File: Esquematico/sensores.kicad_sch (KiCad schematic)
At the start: 2 parts, among them U2 DS18B20

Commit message: sensores 1
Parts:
- added C1: 10u, symbol Device:C
- added C2: 0.1u, symbol Device:C
- added R? (x2): R, symbol Device:R
- added U2: MAX98357AETE+, QFN50P300X300X80-17N, symbol MAX98357AETE_:MAX98357AETE+
- added U?: SR501, symbol Sensor_Luz:SR501
- added U?: SEN0193, symbol Sensor_Luz:SR501
- added U?: APSD-9960-Ar, symbol Sensor_Luz:APSD-9960-Ar
- renumbered U2 to U1
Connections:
- net +5V: now also C1.1, C2.1, U2.2 (GAIN_SLOT), U2.7 (VDD), U2.8 (VDD), U?.1 (Vcc), U?.1 (Vcc)
- net GND: now also C1.2, C2.2, U2.11 (GND), U2.15 (GND), U2.3 (GND), U?.2 (GND), U?.3 (GND), U?.3 (GND)
- new net +3V3: R?.1, R?.1, U?.3 (VCC)
- new net INT: U?.6 (INT)
- new net SCL: R?.2, U?.5 (SCL)
- new net SDA: R?.2, U?.4 (SDA)
- new net VL: U?.1 (VL)
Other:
- note added: "Amplificador de sonido"
- note added: "Sensor de humedad"
- note added: "Sensor de luz"
- note added: "Sensor de moviemiento"
- moved on the sheet: R1, U1

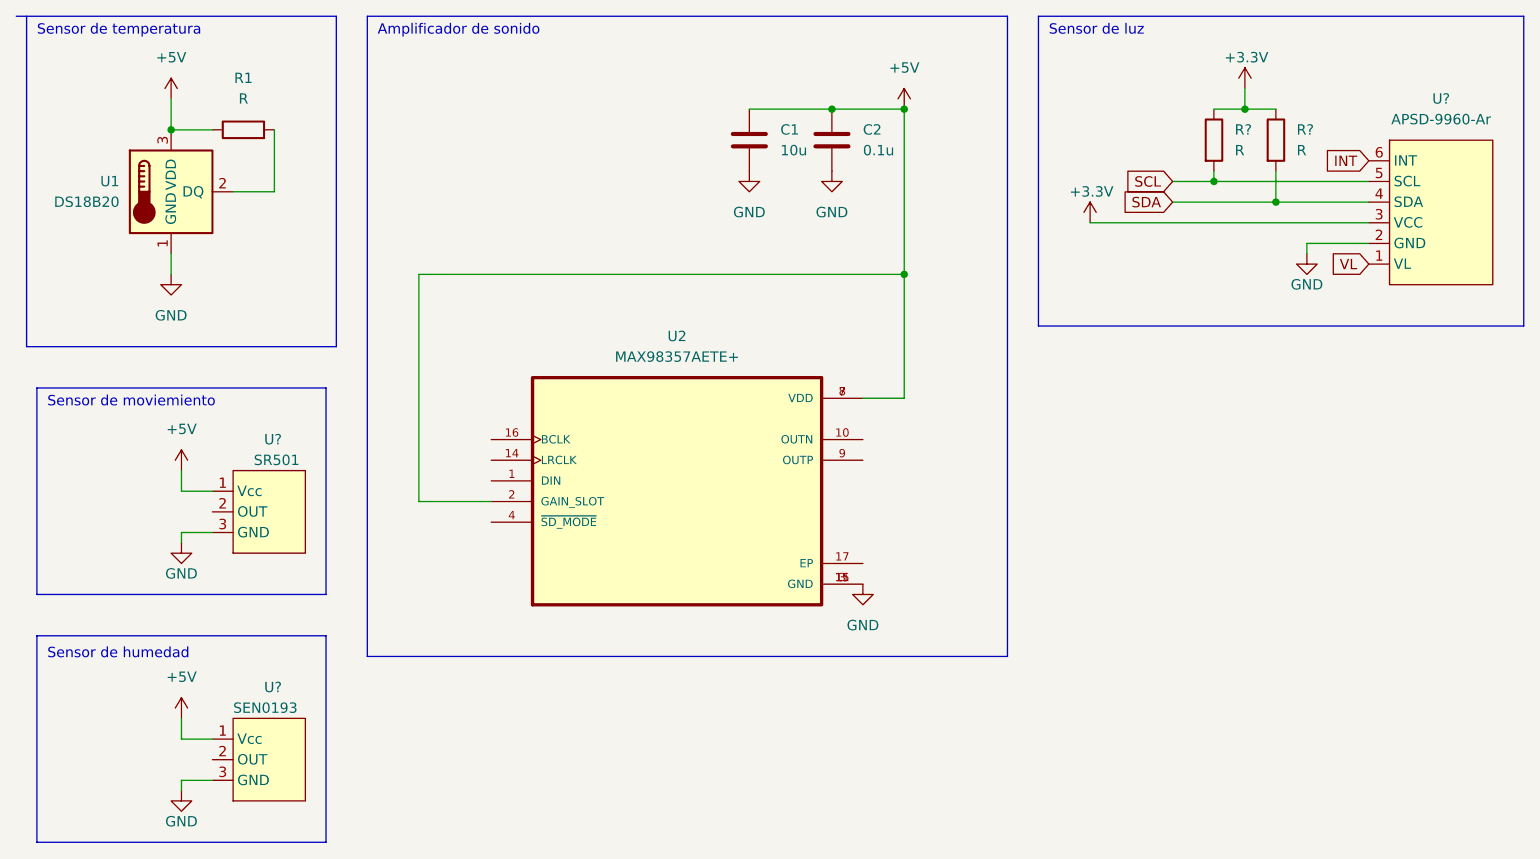
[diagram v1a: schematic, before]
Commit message: Conexion Sensores
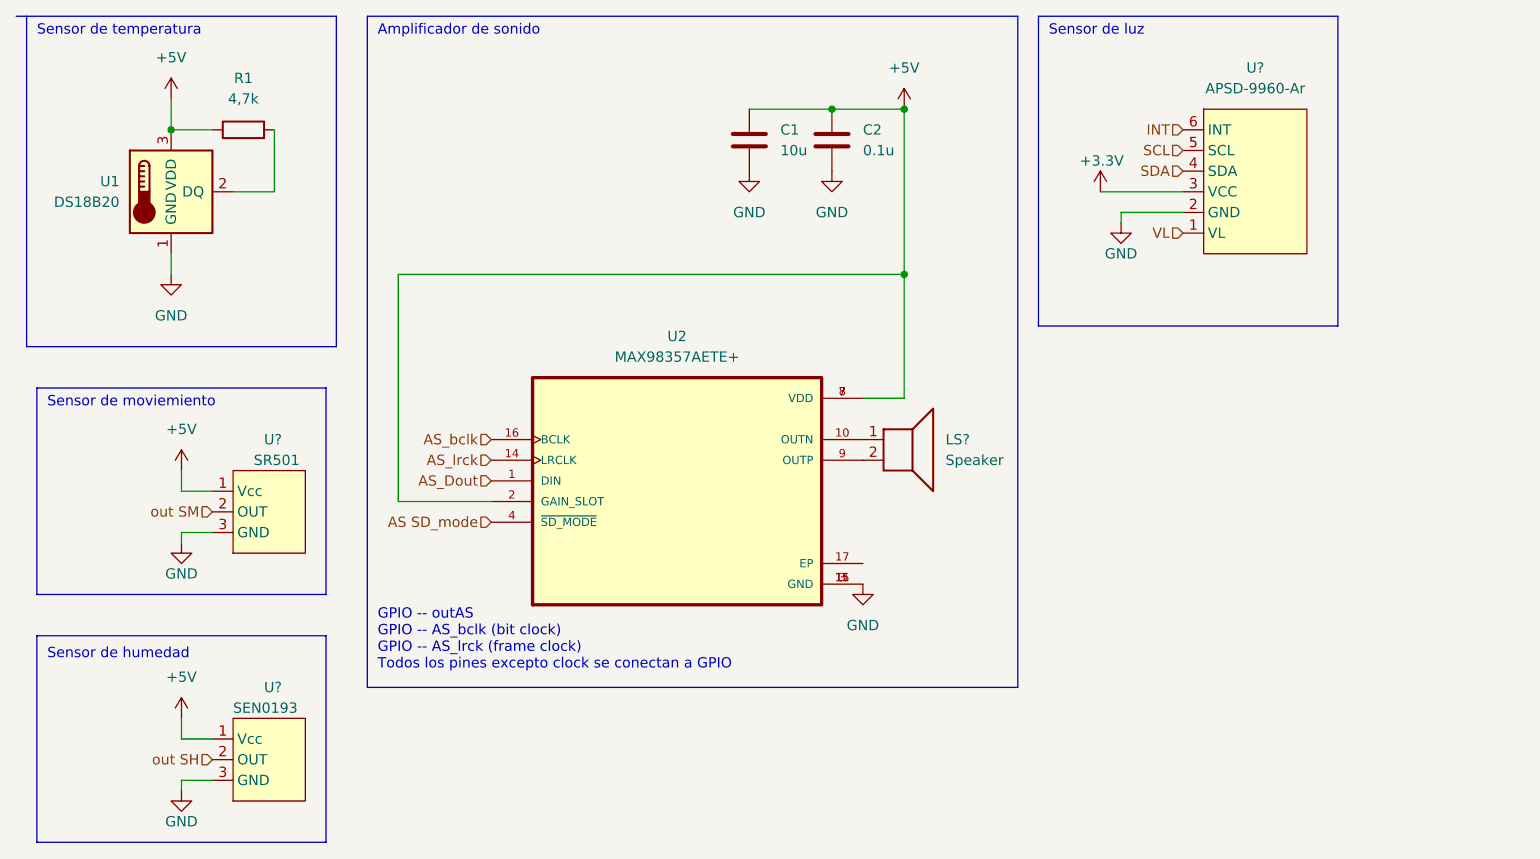
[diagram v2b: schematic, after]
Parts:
- removed R? (x2): R, symbol Device:R
- added LS?: Speaker, symbol Device:Speaker
- R1: value R -> 4,7k
- U?: footprint (none) -> Connector_JST:JST_PH_B3B-PH-SM4-TB_1x03-1MP_P2.00mm_Vertical
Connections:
- net AS_Dout: now reaches U2.1 (DIN)
- net at U2.10 (OUTN): now also LS?.1
- net AS_lrck: now reaches U2.14 (LRCLK)
- net AS_bclk: now reaches U2.16 (BCLK)
- net AS SD_mode: now reaches U2.4 (~{SD_MODE})
- net at U2.9 (OUTP): now also LS?.2
- net out SM: now reaches U?.2 (OUT)
- net out SH: now reaches U?.2 (OUT)
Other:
- note added: "GPIO -- outAS GPIO -- AS_bclk (bit clock) GPIO -- AS_lrck (frame clock) Todos los pines excepto clock se conectan a GPIO"
- moved on the sheet: U?

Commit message: actualizacion huellas resitencias y capacitorees
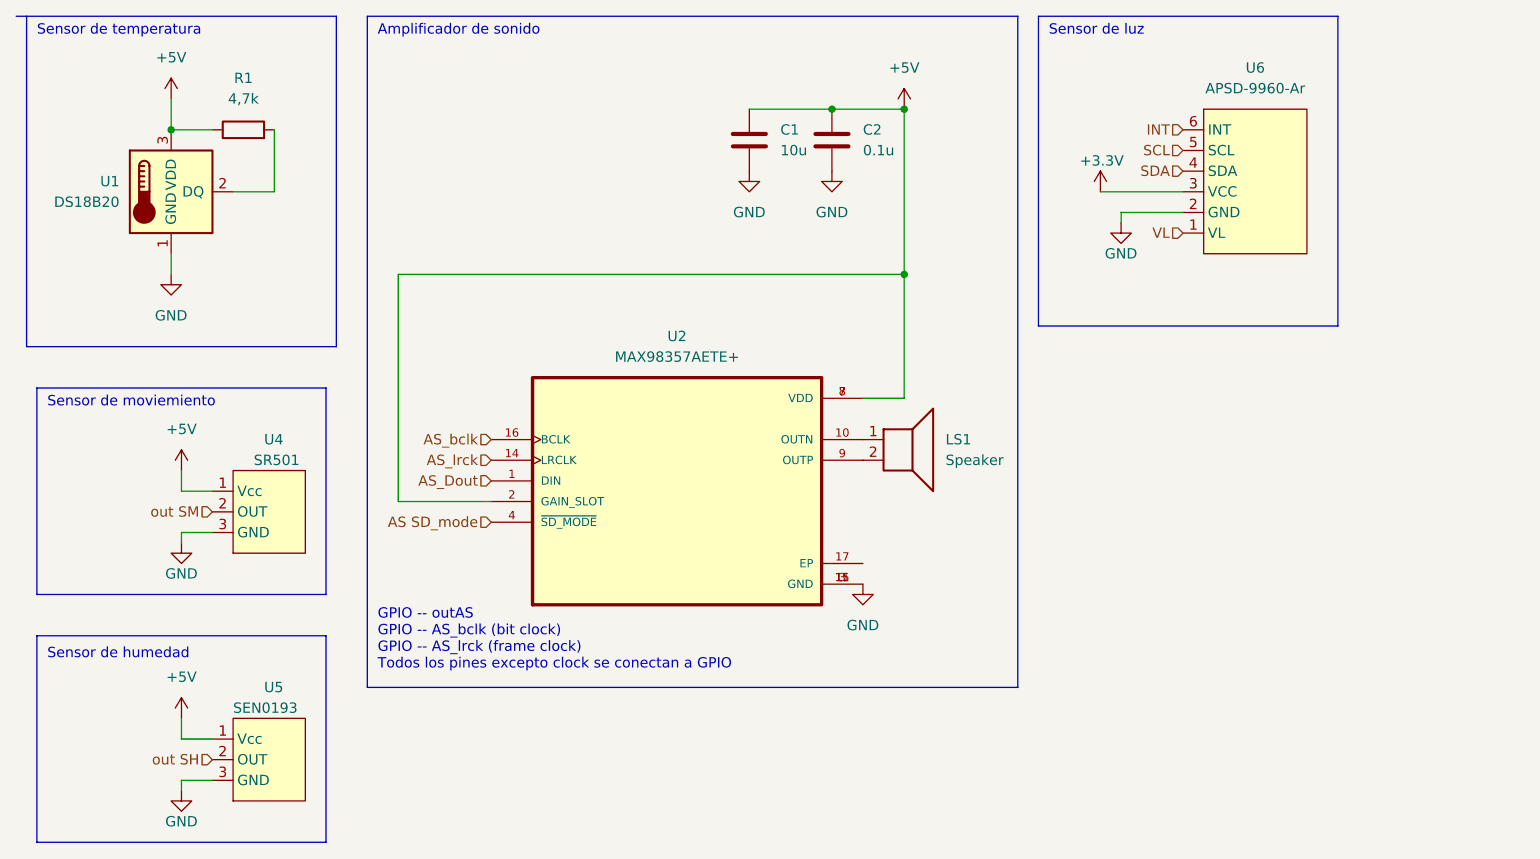
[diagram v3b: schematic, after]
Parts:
- C1, C2: footprint (none) -> Capacitor_SMD:C_0805_2012Metric_Pad1.18x1.45mm_HandSolder
- R1: footprint (none) -> Resistor_SMD:R_0805_2012Metric_Pad1.20x1.40mm_HandSolder
- gave numbers to parts that had none: 4
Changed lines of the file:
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@@
   (symbol (lib_id "power:+5V") (at 39.37 105.41 0) (unit 1)
     (in_bom yes) (on_board yes) (fields_autoplaced)
-    (property "Reference" "#PWR?" (id 0) (at 39.37 109.22 0)
+    (property "Reference" "#PWR0128" (id 0) (at 39.37 109.22 0)
       (effects (font (size 1.27 1.27)) hide)
     )
@@
     (property "Reference" "R1" (id 0) (at 46.99 26.67 90))
     (property "Value" "4,7k" (id 1) (at 46.99 29.21 90))
-    (property "Footprint" "" (id 2) (at 46.99 34.798 90)
+    (property "Footprint" "Resistor_SMD:R_0805_2012Metric_Pad1.20x1.40mm_HandSolder" (id 2) (at 46.99 34.798 90)
       (effects (font (size 1.27 1.27)) hide)
     )
@@
   (symbol (lib_id "power:GND") (at 39.37 114.3 0) (unit 1)
     (in_bom yes) (on_board yes)
-    (property "Reference" "#PWR?" (id 0) (at 39.37 120.65 0)
+    (property "Reference" "#PWR0127" (id 0) (at 39.37 120.65 0)
       (effects (font (size 1.27 1.27)) hide)
     )
@@
       (effects (font (size 1.27 1.27)) (justify left))
     )
-    (property "Footprint" "" (id 2) (at 110.1852 38.1 0)
+    (property "Footprint" "Capacitor_SMD:C_0805_2012Metric_Pad1.18x1.45mm_HandSolder" (id 2) (at 110.1852 38.1 0)
       (effects (font (size 1.27 1.27)) hide)
     )
@@
   (symbol (lib_id "power:GND") (at 123.19 88.9 0) (unit 1)
     (in_bom yes) (on_board yes) (fields_autoplaced)
-    (property "Reference" "#PWR?" (id 0) (at 123.19 95.25 0)
+    (property "Reference" "#PWR0122" (id 0) (at 123.19 95.25 0)
       (effects (font (size 1.27 1.27)) hide)
     )
@@
       (effects (font (size 1.27 1.27)) (justify left))
     )
-    (property "Footprint" "" (id 2) (at 120.3452 38.1 0)
+    (property "Footprint" "Capacitor_SMD:C_0805_2012Metric_Pad1.18x1.45mm_HandSolder" (id 2) (at 120.3452 38.1 0)
       (effects (font (size 1.27 1.27)) hide)
     )
@@
   (symbol (lib_id "Sensor_Luz:SR501") (at 50.8 74.93 0) (mirror y) (unit 1)
     (in_bom yes) (on_board yes)
-    (property "Reference" "U?" (id 0) (at 49.53 71.12 0)
+    (property "Reference" "U4" (id 0) (at 49.53 71.12 0)
       (effects (font (size 1.27 1.27)) (justify right))
     )
@@
   (symbol (lib_id "Sensor_Luz:SR501") (at 50.8 105.41 0) (mirror y) (unit 1)
     (in_bom yes) (on_board yes)
-    (property "Reference" "U?" (id 0) (at 49.53 101.6 0)
+    (property "Reference" "U5" (id 0) (at 49.53 101.6 0)
       (effects (font (size 1.27 1.27)) (justify right))
     )
@@
   (symbol (lib_id "power:+3.3V") (at 152.4 40.64 0) (unit 1)
     (in_bom yes) (on_board yes)
-    (property "Reference" "#PWR?" (id 0) (at 152.4 44.45 0)
+    (property "Reference" "#PWR0123" (id 0) (at 152.4 44.45 0)
       (effects (font (size 1.27 1.27)) hide)
     )
@@
   (symbol (lib_id "Device:Speaker") (at 128.27 71.12 0) (unit 1)
     (in_bom yes) (on_board yes) (fields_autoplaced)
-    (property "Reference" "LS?" (id 0) (at 133.35 71.1199 0)
+    (property "Reference" "LS1" (id 0) (at 133.35 71.1199 0)
       (effects (font (size 1.27 1.27)) (justify left))
     )
@@
   (symbol (lib_id "power:+5V") (at 39.37 74.93 0) (unit 1)
     (in_bom yes) (on_board yes) (fields_autoplaced)
-    (property "Reference" "#PWR?" (id 0) (at 39.37 78.74 0)
+    (property "Reference" "#PWR0125" (id 0) (at 39.37 78.74 0)
       (effects (font (size 1.27 1.27)) hide)
     )
@@
   (symbol (lib_id "power:GND") (at 109.22 38.1 0) (unit 1)
     (in_bom yes) (on_board yes) (fields_autoplaced)
-    (property "Reference" "#PWR?" (id 0) (at 109.22 44.45 0)
+    (property "Reference" "#PWR0119" (id 0) (at 109.22 44.45 0)
       (effects (font (size 1.27 1.27)) hide)
     )
@@
   (symbol (lib_id "Sensor_Luz:APSD-9960-Ar") (at 171.45 52.07 0) (mirror x) (unit 1)
     (in_bom yes) (on_board yes) (fields_autoplaced)
-    (property "Reference" "U?" (id 0) (at 171.45 25.4 0))
+    (property "Reference" "U6" (id 0) (at 171.45 25.4 0))
     (property "Value" "APSD-9960-Ar" (id 1) (at 171.45 27.94 0))
     (property "Footprint" "" (id 2) (at 171.45 52.07 0)
@@
   (symbol (lib_id "power:GND") (at 39.37 83.82 0) (unit 1)
     (in_bom yes) (on_board yes)
-    (property "Reference" "#PWR?" (id 0) (at 39.37 90.17 0)
+    (property "Reference" "#PWR0126" (id 0) (at 39.37 90.17 0)
       (effects (font (size 1.27 1.27)) hide)
     )
@@
   (symbol (lib_id "power:GND") (at 119.38 38.1 0) (unit 1)
     (in_bom yes) (on_board yes) (fields_autoplaced)
-    (property "Reference" "#PWR?" (id 0) (at 119.38 44.45 0)
+    (property "Reference" "#PWR0120" (id 0) (at 119.38 44.45 0)
       (effects (font (size 1.27 1.27)) hide)
     )
@@
   (symbol (lib_id "power:GND") (at 154.94 44.45 0) (unit 1)
     (in_bom yes) (on_board yes)
-    (property "Reference" "#PWR?" (id 0) (at 154.94 50.8 0)
+    (property "Reference" "#PWR0124" (id 0) (at 154.94 50.8 0)
       (effects (font (size 1.27 1.27)) hide)
     )
@@
   (symbol (lib_id "power:+5V") (at 128.27 30.48 0) (unit 1)
     (in_bom yes) (on_board yes) (fields_autoplaced)
-    (property "Reference" "#PWR?" (id 0) (at 128.27 34.29 0)
-      (effects (font (size 1.27 1.27)) hide)
-    )
+    (property "Reference" "#PWR0121" (id 0) (at 128.27 34.29 0)
+      (effects (font (size 1.27 1.27)) hide)
+    )
